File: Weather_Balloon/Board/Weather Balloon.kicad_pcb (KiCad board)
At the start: 2 copper layers, 182.4 x 96.5 mm, 200 parts, among them IC1 ATTINY85-P, IC2 ATMEGA2560-A, M1 MountingHole_2.5mm, M2 MountingHole_2.5mm, M3 MountingHole_2.5mm, M4 MountingHole_2.5mm, P1 85_PRGM, P10 SERIAL, P11 UV_ADC, P12 Custom_HEAT, P13 SHT31_HEAT, P14 GPS_HEAT, P15 UV_HEAT, P16 TSL2561_HEAT, P17 LSM9DS1, P18 PIEZO, P19 MICRO_SD_CARD, P2 ADC_AUX, P20 LANDING_LED, P21 DS18B20, P22 RADIO, P23 EXT_SENSORS, P26 MS5607, P27 GPS, P28 5V_BOOST, P3 SENSOR_I2C, P4 2560_RESET, P5 2560_SCK, P6 2560_MOSI, P7 2560_MISO, P8 85_RESET, P9 Geiger, Q1 PSMN9R1-30YL,115, Q10 PSMN9R1-30YL,115, Q11 PSMN9R1-30YL,115, Q12 PSMN9R1-30YL,115, Q13 PSMN9R1-30YL,115, Q14 PSMN9R1-30YL,115, Q15 PSMN9R1-30YL,115, Q16 PSMN9R1-30YL,115, Q17 PSMN9R1-30YL,115, Q2 PSMN9R1-30YL,115, Q3 PSMN9R1-30YL,115, Q4 PSMN9R1-30YL,115, Q5 PSMN9R1-30YL,115, Q6 PSMN9R1-30YL,115, Q7 PSMN9R1-30YL,115, Q8 PSMN9R1-30YL,115, Q9 PSMN9R1-30YL,115, SW1 SILENCE, U1 MAX6107EUR, U10 AT25_EEPROM, U11 AT25_EEPROM, U12 AT25_EEPROM, U13 AT25_EEPROM, U14 AT25_EEPROM, U15 AT25_EEPROM, U16 LD1117S33TR, U2 BILEVEL_SHIFT, U3 BILEVEL_SHIFT, U4 DS3231, U5 FUEL_GAUGE, U6 AT25_EEPROM, U7 AT25_EEPROM, U8 AT25_EEPROM, U9 AT25_EEPROM, Y1 16Mhz

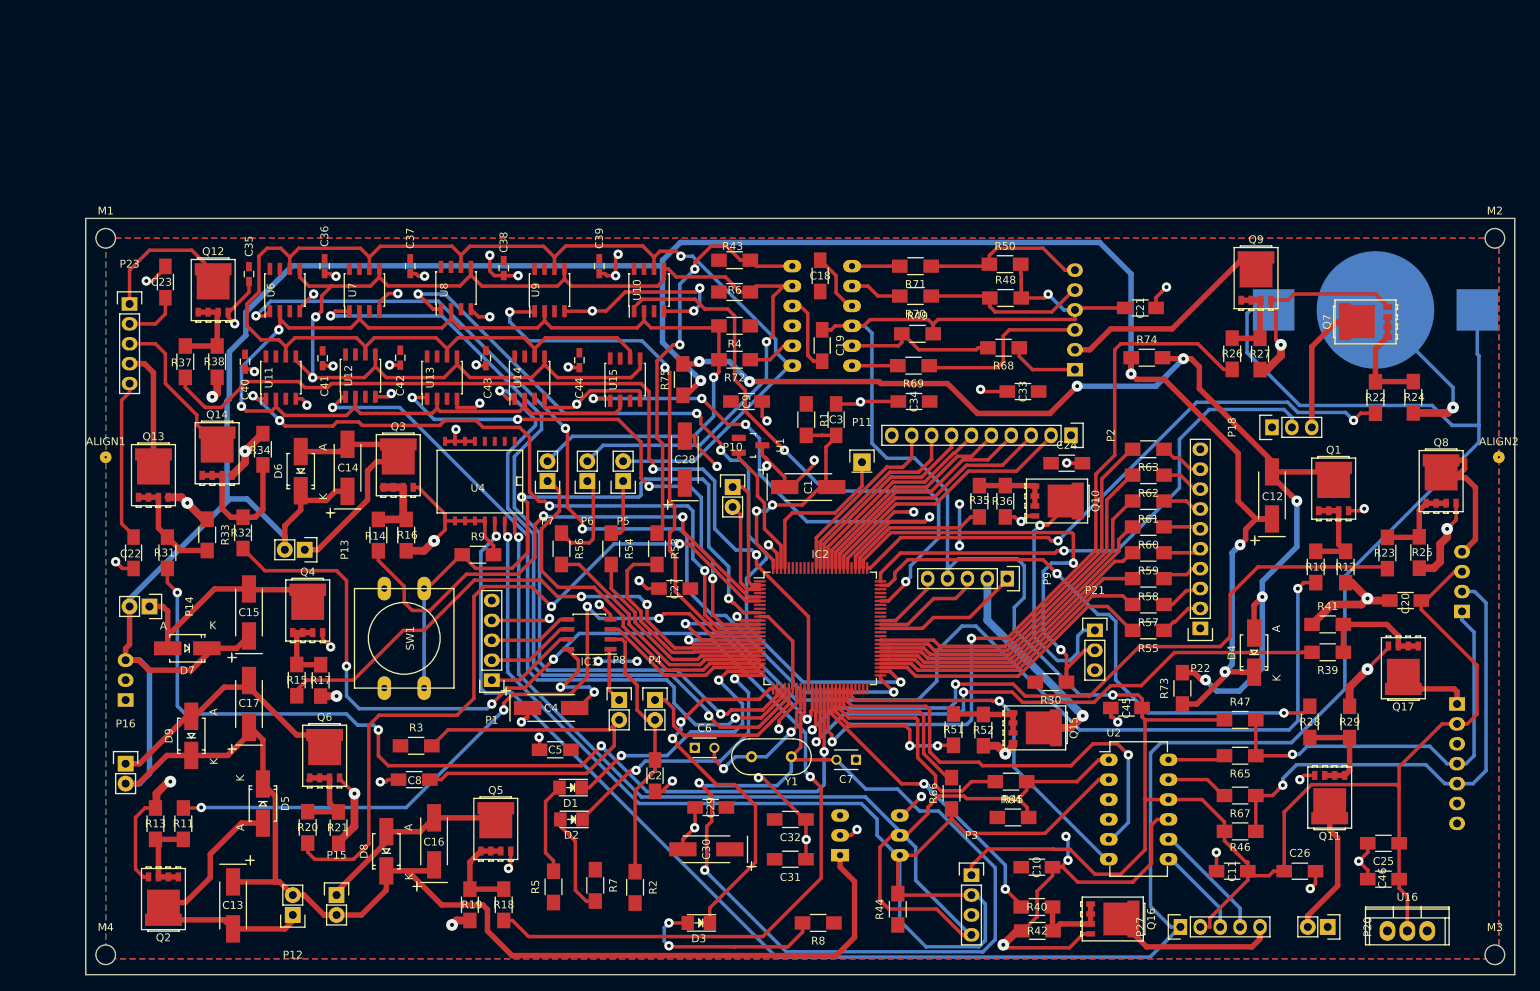
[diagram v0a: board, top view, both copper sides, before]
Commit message: Updated PCB board for larger traces and more compact design.
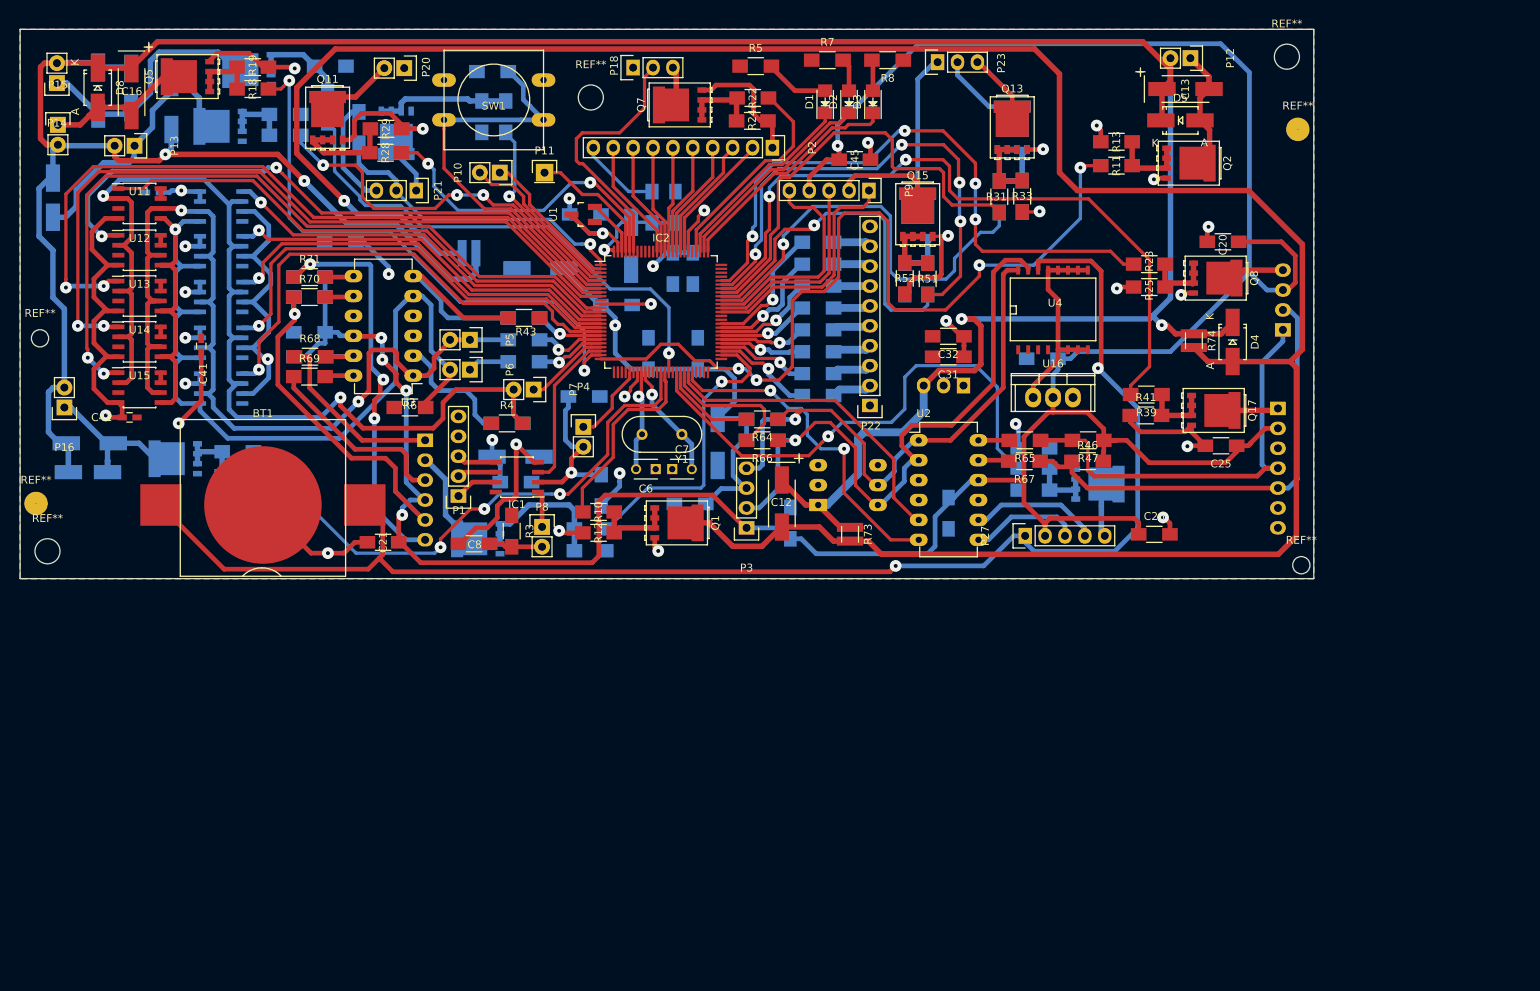
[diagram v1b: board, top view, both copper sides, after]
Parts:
- removed ALIGN1, ALIGN2: Measurement_Point_Round-TH_Small, Personal:Measurement_Point_Round-TH_Small_0.3
- removed C35, C36, C37, C38, C39, C40, C44: 4.7uF, Capacitors_SMD:C_0603_HandSoldering
- removed M1, M2, M3, M4: MountingHole_2.5mm, Mounting_Holes:MountingHole_2.5mm
- added REF**: MountingHole_3.2mm_M3, Mounting_Holes:MountingHole_3.2mm_M3, F.Cu at (52.3, 90.2)
- added REF**: MountingHole_3.2mm_M3, Mounting_Holes:MountingHole_3.2mm_M3, F.Cu at (210.4, 27.1)
- added REF**: MountingHole_3.2mm_M3, Mounting_Holes:MountingHole_3.2mm_M3, F.Cu at (121.6, 32.3)
- added REF**: MountingHole_2.2mm_M2, Mounting_Holes:MountingHole_2.2mm_M2, F.Cu at (212.3, 92.0)
- added REF**: MountingHole_2.2mm_M2, Mounting_Holes:MountingHole_2.2mm_M2, F.Cu at (51.3, 63.1)
- added REF**: Measurement_Point_Round-TH_Big, Measurement_Points:Measurement_Point_Round-TH_Big, F.Cu at (211.8, 36.4)
- added REF**: Measurement_Point_Round-TH_Big, Measurement_Points:Measurement_Point_Round-TH_Big, F.Cu at (50.8, 84.1)
- BT1, U3: moved to F.Cu
- C1, C10, C11, C14, C15, C17, C18, C19, C2, C22, C23, C24, C27, C28, C29, C3, C30, C33, C34, C4, C43, C46, C5, C9, D6, D7, D9, Q10, Q12, Q14, Q16, Q3, Q4, Q6, Q9, R1, R14, R15, R16, R17, R2, R20, R21, R26, R27, R30, R32, R34, R35, R36, R37, R38, R40, R42, R44, R45, R48, R49, R50, R53, R54, R55, R56, R57, R58, R59, R60, R61, R62, R63, R72, R9, U10, U6, U7, U8, U9: moved to B.Cu
- P23: footprint Pin_Headers:Pin_Header_Straight_1x05 -> Pin_Headers:Pin_Header_Straight_1x03
- R73, R74: footprint Resistors_SMD:R_1206_HandSoldering -> Personal:R_1206_WIDE
- R75: footprint Resistors_SMD:R_1206_HandSoldering -> Personal:R_1206_WIDE; moved to B.Cu
- moved Q2 161.1 mm to (197.9, 40.7), turned to 270 degrees
- moved P20 160.9 mm to (97.8, 28.6)
- moved C13 160.1 mm to (197.5, 31.2), turned to 0 degrees
- moved P12 158.4 mm to (198.1, 27.3), turned to 270 degrees
- moved Q11 154.5 mm to (88.0, 34.9), turned to 0 degrees
- moved R13 150.4 mm to (188.7, 38.0), turned to 180 degrees
- moved D5 146.0 mm to (196.8, 35.2), turned to 0 degrees
- moved R11 145.7 mm to (188.7, 41.0), turned to 180 degrees
- moved R29 144.4 mm to (95.5, 36.3), turned to 180 degrees
- moved BT1 144.2 mm to (79.8, 84.3)
- moved R28 138.5 mm to (95.4, 39.4), turned to 0 degrees
- moved Q13 118.2 mm to (175.4, 36.1)
- moved R31 115.5 mm to (173.7, 45.0)
- moved P28 114.2 mm to (169.2, 69.1), turned to 90 degrees
- moved R30 113.2 mm to (92.0, 36.2), turned to 90 degrees
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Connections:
- C22 pad 1: Net-(C22-Pad1) -> Vcc_1
- C23 pad 1: Net-(C23-Pad1) -> +3V3
- IC2 pad 1: (no net) -> DS18B20_DATA
- IC2 pad 12: AT25_CS_9 -> AT25_CS_10
- IC2 pad 14: AT25_CS_7 -> AT25_CS_1
- IC2 pad 15: Custom_Heat -> AT25_CS_6
- IC2 pad 16: Main_Heat -> AT25_CS_2
- IC2 pad 17: UV_Heat -> AT25_CS_7
- IC2 pad 18: GPS_Heat -> AT25_CS_3
- IC2 pad 24: Net-(D1-Pad1) -> UV_Heat
- IC2 pad 25: Net-(D2-Pad1) -> Custom_Heat
- IC2 pad 26: Net-(D3-Pad1) -> (no net)
- IC2 pad 27: AT25_CS_6 -> (no net)
- IC2 pad 28: AT25_CS_4 -> (no net)
- IC2 pad 29: AT25_CS_5 -> (no net)
- IC2 pad 35: UV_POWER -> (no net)
- IC2 pad 36: SHT31_RESET -> (no net)
- IC2 pad 37: DOF_POWER -> (no net)
- IC2 pad 38: MS5607_POWER -> TSL2561_Heat
- IC2 pad 39: TSL2561_POWER -> Main_Heat
- IC2 pad 4: (no net) -> DS18B20_PWR
- IC2 pad 40: SD_POWER -> GPS_Heat
- IC2 pad 41: GPS_POWER -> (no net)
- IC2 pad 42: GEIGER_POWER -> GPS_POWER
- IC2 pad 51: AT25_CS_1 -> (no net)
- IC2 pad 52: AT25_CS_2 -> SD_POWER
- IC2 pad 6: TSL2561_Heat -> Net-(IC2-Pad6)
- IC2 pad 66: (no net) -> SHT31_RESET
- IC2 pad 67: (no net) -> UV_POWER
- IC2 pad 68: (no net) -> TSL2561_POWER
- IC2 pad 69: (no net) -> MS5607_POWER
- IC2 pad 7: (no net) -> AT25_CS_4
- IC2 pad 70: AT25_CS_3 -> GEIGER_POWER
- IC2 pad 71: (no net) -> DOF_POWER
- IC2 pad 74: LANDING_LED -> (no net)
- IC2 pad 75: PIEZO -> (no net)
- IC2 pad 76: PIEZO_PWR -> Net-(D3-Pad1)
- IC2 pad 77: DS18B20_DATA -> Net-(D2-Pad1)
- IC2 pad 78: DS18B20_PWR -> Net-(D1-Pad1)
- IC2 pad 79: AT25_CS_10 -> PIEZO_PWR
- IC2 pad 8: (no net) -> AT25_CS_9
- IC2 pad 9: Net-(IC2-Pad9) -> AT25_CS_5
- IC2 pad 95: (no net) -> PIEZO
- IC2 pad 96: (no net) -> LANDING_LED
- P23 pad 2: Net-(C23-Pad1) -> SHT_31_PWR
- P23 pad 3: SHT_31_PWR -> Net-(P23-Pad3)
- P5 pad 1: Net-(P5-Pad1) -> SCK
- Q13 pad 2: Net-(P23-Pad4) -> Net-(P23-Pad3)
- R54 pad 1: Net-(P5-Pad1) -> SCK
- R9 pad 1: Net-(IC2-Pad9) -> Net-(IC2-Pad6)
- SW1 pad 1: Net-(IC2-Pad9) -> Net-(IC2-Pad6)
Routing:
- net GND: track 466.8 -> 242.6 mm, vias 75 -> 24
- net Net-(C12-Pad2): track 150.0 -> 317.4 mm, vias 7 -> 1
- net Vcc_1: track 25.9 -> 174.0 mm, vias 2 -> 13
- net Net-(C7-Pad2): track 119.2 -> 14.8 mm, vias 2 -> 1
- net Main_Heat: track 124.2 -> 24.8 mm, vias 2 -> 0
- net CR2032_POS: track 277.7 -> 186.6 mm, vias 1 -> 2
- net Net-(IC2-Pad9): track 83.0 -> 0.00 mm, vias 2 -> 0
- net SCL_5: track 153.4 -> 71.9 mm
- net SDA_5: track 156.9 -> 81.6 mm
- net UV_POWER: track 115.1 -> 45.3 mm, vias 2 -> 1
- net AT25_CS_1: track 118.0 -> 52.3 mm, vias 4 -> 1
- net +BATT: track 480.6 -> 415.3 mm
- net TSL2561_POWER: track 121.8 -> 57.2 mm, vias 4 -> 0
- net +3V3: track 308.2 -> 371.6 mm, vias 2 -> 5
- net SCK: track 184.8 -> 122.5 mm, vias 1 -> 2
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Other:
- board size 182.4 x 96.5 mm -> 165.1 x 70.1 mm
- net class Default: clearance 0.001 -> 0.05; trace_width 0.45 -> 0.6; via_dia 1.2 -> 1.5
- net class Heat: clearance 0.001 -> 0.05; via_dia 1.4 -> 1.5
- net class Micro added: clearance 0.05, trace_width 0.42, via_dia 1.5, via_drill 0.5
- net class Power: clearance 0.001 -> 0.05; trace_width 0.45 -> 0.6; via_dia 1.2 -> 1.5
- net class SOIC added: clearance 0.05, trace_width 0.6, via_dia 1.5, via_drill 0.5
- rule trace_clearance: 0.001 -> 0.05

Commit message: PID control and beginning of altitude alarm.
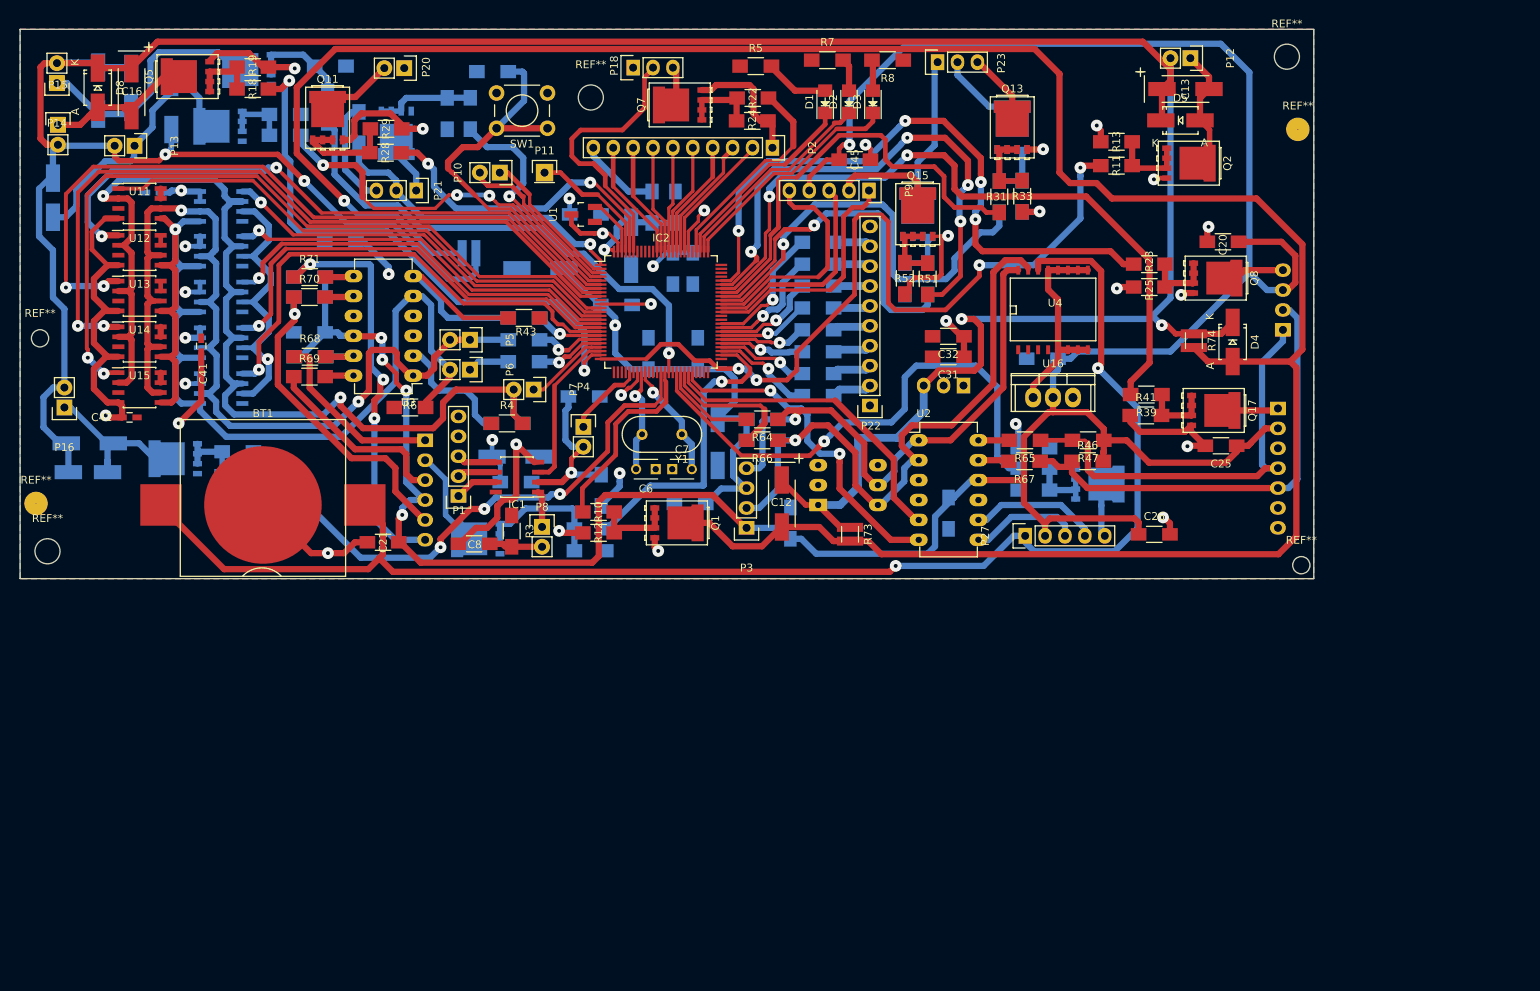
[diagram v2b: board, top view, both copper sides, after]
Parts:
- SW1: footprint Buttons_Switches_ThroughHole:SW_PUSH-12mm -> Buttons_Switches_ThroughHole:SW_PUSH_6mm
- moved SW1 7.75 mm to (116.1, 36.2)
- moved R35 4.54 mm to (106.2, 34.4)
- moved R36 4.44 mm to (103.3, 34.4)
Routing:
- net DS18B20_PWR: track 24.9 -> 30.0 mm
- net Net-(Q10-Pad1): track 17.2 -> 12.7 mm
- net MISO: track 139.4 -> 143.0 mm
- net GEIGER_POWER: track 63.8 -> 67.0 mm
- net DOF_POWER: track 79.1 -> 82.2 mm
- net PIEZO: track 33.6 -> 36.3 mm
- net Custom_Heat: track 108.0 -> 105.5 mm
- net Net-(IC2-Pad6): track 53.1 -> 51.5 mm
- net +BATT: track 415.3 -> 416.8 mm
- net SCK: track 122.5 -> 123.6 mm
- net GEIGER_Y: track 26.1 -> 27.2 mm
- net TSL2561_POWER: track 57.2 -> 56.1 mm
- net SS_3.3: track 53.6 -> 54.4 mm
- net UV_Heat: track 72.8 -> 73.6 mm
- net SDA_5: track 81.6 -> 80.9 mm
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
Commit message: After flight data retrieval
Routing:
- net SCK: track 123.6 -> 121.0 mm
